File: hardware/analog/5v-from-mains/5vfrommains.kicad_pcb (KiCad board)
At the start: 2 copper layers, 70.8 x 100 mm, 22 parts, among them J1 Conn_WallSocket_Earth, J2 Conn_WallSocket_Earth, U7 LM7805_TO220

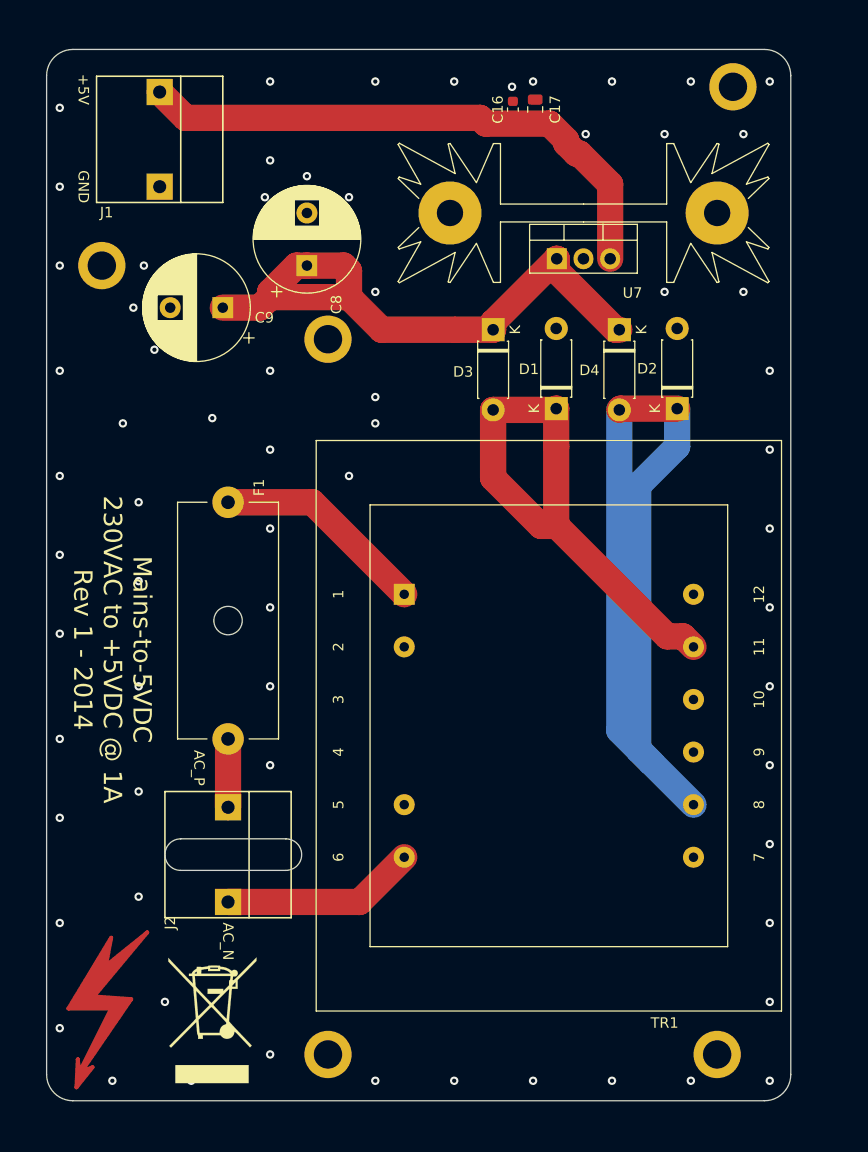
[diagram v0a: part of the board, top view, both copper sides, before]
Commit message: Added voltage reference REF5020 datasheet
Started work on HW rev 2 of electro load and 5v-from-mains - rev 1 contained misaligned footprints.
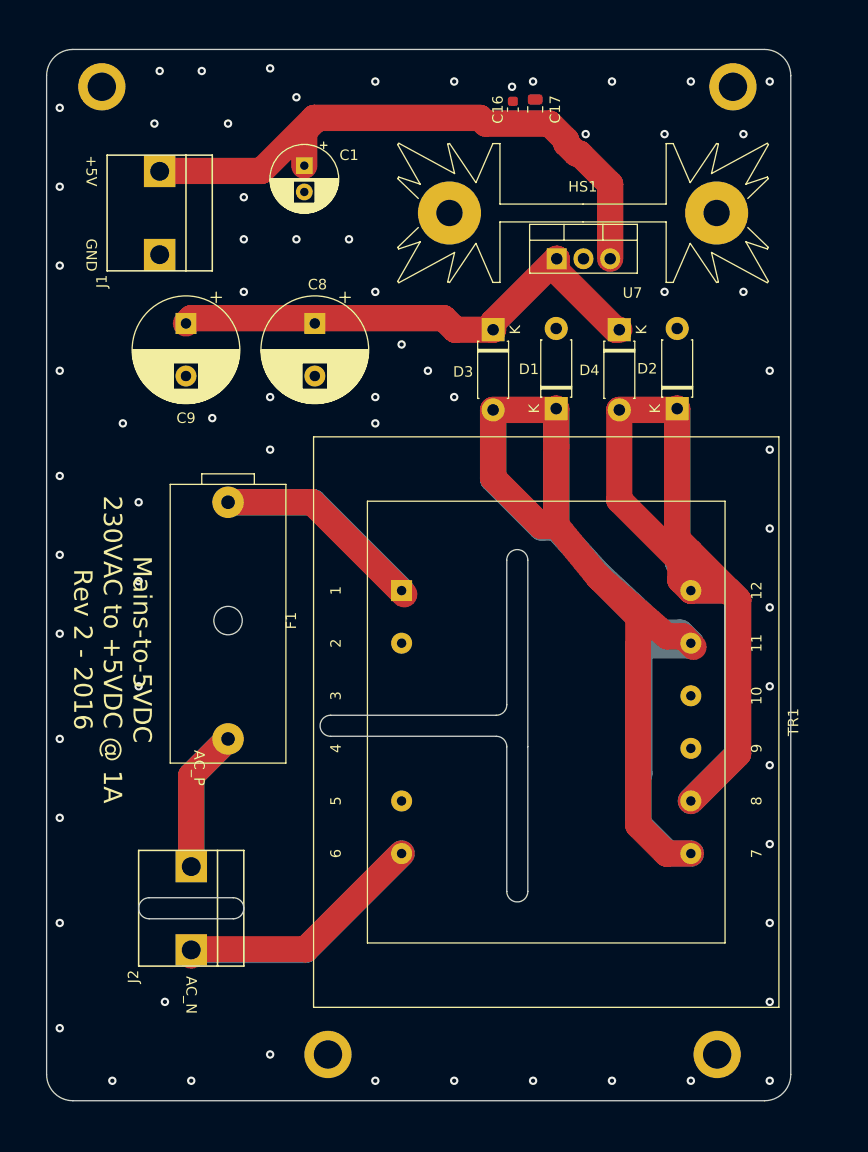
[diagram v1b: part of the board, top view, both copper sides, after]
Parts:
- removed the REF** at (224.8, 60.0)
- removed the REF** at (189.5, 136.8)
- removed the REF** at (179.0, 135.2)
- removed the REF** at (218.8, 138.0)
- removed the REF** at (200.5, 72.0)
- added C1: 10u, Capacitor_THT:CP_Radial_D6.3mm_P2.50mm, F.Cu at (198.2, 55.5)
- added HS1: Heatsink, athir:Heatsink_Fischer_SK104-STC-STIC_35x13mm_2xDrill2.5mm, F.Cu at (224.8, 60.0)
- F1: footprint Fuse:Fuseholder_Cylinder-5x20mm_Schurter_0031_8201_Horizontal_Open -> athir:KK-Fuseholder
- J1, J2: footprint athir:230VAC_PLUG -> athir:Molex-KK-396-5277
- TR1: value Transformer-230vac-9vac-1va -> Transformer_1P_2S
- moved REF** 17.0 mm to (179.0, 48.0)
- moved F1 11.3 mm to (191.0, 98.8)
- moved J1 7.00 mm to (184.5, 60.0)
- moved J2 6.19 mm to (187.5, 126.1)
- moved C8 5.55 mm to (199.2, 70.5), turned to 270 degrees
- moved C9 3.81 mm to (187.0, 70.5), turned to 270 degrees
- moved TR1 0.43 mm to (207.5, 95.9)
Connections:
- TR1 pad 12: (no net) -> Net-(D2-Pad1)
- TR1 pad 7: (no net) -> Net-(D1-Pad1)
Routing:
- net Net-(D1-Pad1): track 49.4 -> 172.9 mm
- net Net-(D2-Pad1): track 81.7 -> 127.7 mm
- net Net-(J2-Pad2): track 18.5 -> 47.8 mm
- net Net-(F1-Pad2): track 6.50 -> 26.6 mm
- net Net-(F1-Pad1): track 20.4 -> 40.4 mm
- net Net-(C8-Pad1): track 57.8 -> 48.5 mm
- net +5V: track 53.7 -> 59.7 mm
- net GND: vias 67 -> 66
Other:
- outline, holes or cut-outs redrawn
- board text added: "Mains-to-5VDC 230VAC to +5VDC @ 1A Rev 2 - 2016"
- board text removed: "Mains-to-5VDC 230VAC to +5VDC @ 1A Rev 1 - 2014"
